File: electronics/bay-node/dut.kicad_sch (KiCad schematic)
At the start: 26 parts, among them J5 AUX, J6 CAM, Q2 2N7002, Q3 2N7002, U10 INA226AIDGSR, U9 TPS2553DBVR

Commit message: Bay node v0.4: In2 power only, re-placed, SMD JST PH, new GPIO map
Fabio's second round: signals / GND / power / signals.  With no signal
on In2, v0.3's placement left 13-18 connections unrouted, mostly GPIOs
leaving the module's left column for the right half.  Connectors and
module stay put; the DUT power block moves to the top right, LDO and
buttons to the top left, the muxes under the module, and each GPIO sits
on the module edge facing its destination (firmware devicetree, README
pin table and docs follow; check_pinmap.py passes).

pcbgen: fanout_nets gives every GND/supply pin its own locked via to
its plane before routing.  USB HS pairs redrawn for the new geometry
(J3 -> J4 skew 0.1 mm).  J1/J2/J5/J6 are now S*B-PH-SM4-TB, placed by
JLC (24 V and GND on solid islands with 4 vias each); UART test pads on
the bottom side.  J5 is a JST PH 6 (Fabio: SH too small).

ERC 0, DRC 0 errors / 0 warnings / 0 unconnected, parity 0 (Konnect).

Co-Authored-By: Claude Opus 5.5 <noreply@anthropic.com>
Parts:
- J5: footprint Connector_JST:JST_SH_SM06B-SRSS-TB_1x06-1MP_P1.00mm_Horizontal -> Connector_JST:JST_PH_S6B-PH-SM4-TB_1x06-1MP_P2.00mm_Horizontal; symbol Connector_Generic_MountingPin:Conn_01x06_MountingPin -> Connector_Generic:Conn_01x06; Alternative JST SM06B-SRSS-TB(LF)(SN) C160405 -> (none); LCSC C56123098 -> C265405; MPN XY-SM06B-SRSS-TB -> S6B-PH-SM4-TB(LF)(SN); Manufacturer XYECONN -> JST
- J6: footprint Connector_JST:JST_PH_S2B-PH-K_1x02_P2.00mm_Horizontal -> Connector_JST:JST_PH_S2B-PH-SM4-TB_1x02-1MP_P2.00mm_Horizontal; LCSC C173752 -> C295747; MPN S2B-PH-K-S(LF)(SN) -> S2B-PH-SM4-TB(LF)(SN)
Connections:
- net GND: no longer J5.MP (MountPin)
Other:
- note added: "AUX: UART + open-drain RESET / BOOT towards the DUT (JST PH 6)"
- note removed: "AUX: UART + open-drain RESET / BOOT towards the DUT (JST SH 6)"
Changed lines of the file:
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@@
 	(title_block
 		(title "Bay node — DUT power switch, monitor, AUX and camera power")
-		(rev "0.3")
+		(rev "0.4")
 		(company "hw-testing-rack")
 		(comment 1 "ESP32-S3 USB/IP host for one bay of the hw-testing-rack shelf")
@@
 	)
 	(symbol
-		(lib_id "Connector_Generic_MountingPin:Conn_01x06_MountingPin")
+		(lib_id "Connector_Generic:Conn_01x06")
 		(at 269.24 162.56 0)
 		(unit 1)
@@
 			)
 		)
-		(property "Footprint" "Connector_JST:JST_SH_SM06B-SRSS-TB_1x06-1MP_P1.00mm_Horizontal"
+		(property "Footprint" "Connector_JST:JST_PH_S6B-PH-SM4-TB_1x06-1MP_P2.00mm_Horizontal"
 			(at 269.24 162.56 0)
 			(effects
@@
 			)
 		)
-		(property "Description" "JST-SH 6-pin side entry"
+		(property "Description" "JST PH 6-pin, side entry, SMD"
 			(at 269.24 162.56 0)
 			(effects
@@
 			)
 		)
-		(property "MPN" "XY-SM06B-SRSS-TB"
+		(property "MPN" "S6B-PH-SM4-TB(LF)(SN)"
 			(at 269.24 162.56 0)
 			(effects
@@
 			)
 		)
-		(property "Manufacturer" "XYECONN"
-			(at 269.24 162.56 0)
-			(effects
-				(font
-					(size 1.27 1.27)
-				)
-				(hide yes)
-			)
-		)
-		(property "LCSC" "C56123098"
+		(property "Manufacturer" "JST"
 			(at 269.24 162.56 0)
 			(effects
@@
 			)
 		)
-		(property "Alternative" "JST SM06B-SRSS-TB(LF)(SN) C160405"
+		(property "LCSC" "C265405"
 			(at 269.24 162.56 0)
 			(effects
@@
 		(pin "6"
 		)
-		(pin "MP"
-		)
 		(instances
 			(project "bay-node"
@@
 		)
 	)
-	(wire
-		(pts
-			(xy 269.24 175.26)
-			(xy 269.24 177.8)
-		)
-		(stroke
-			(width 0)
-			(type default)
-		)
-	)
-	(symbol
-		(lib_id "power:GND")
-		(at 269.24 177.8 0)
-		(unit 1)
-		(exclude_from_sim no)
-		(in_bom yes)
-		(on_board yes)
-		(dnp no)
-		(fields_autoplaced yes)
-		(property "Reference" "#PWR05010"
-			(at 269.24 177.8 0)
-			(effects
-				(font
-					(size 1.27 1.27)
-				)
-				(hide yes)
-			)
-		)
-		(property "Value" "GND"
-			(at 269.24 181.61 0)
-			(effects
-				(font
-					(size 1.27 1.27)
-				)
-			)
-		)
-		(property "Footprint" ""
-			(at 269.24 177.8 0)
-			(effects
-				(font
-					(size 1.27 1.27)
-				)
-				(hide yes)
-			)
-		)
-		(property "Datasheet" ""
-			(at 269.24 177.8 0)
-			(effects
-				(font
-					(size 1.27 1.27)
-				)
-				(hide yes)
-			)
-		)
-		(property "Description" ""
-			(at 269.24 177.8 0)
-			(effects
-				(font
-					(size 1.27 1.27)
-				)
-				(hide yes)
-			)
-		)
-		(pin "1"
-		)
-		(instances
-			(project "bay-node"
-				(path "/76847c0c-2f76-566c-8109-428b2bf58b3f/a569d74c-9c07-57e9-a349-c34419c82b47"
-					(reference "#PWR05010")
-					(unit 1)
-				)
-			)
-		)
-	)
 	(symbol
 		(lib_id "Device:R")
@@
 		(dnp no)
 		(fields_autoplaced yes)
-		(property "Reference" "#PWR05011"
+		(property "Reference" "#PWR05010"
 			(at 220.98 182.88 0)
 			(effects
@@
 			(project "bay-node"
 				(path "/76847c0c-2f76-566c-8109-428b2bf58b3f/a569d74c-9c07-57e9-a349-c34419c82b47"
-					(reference "#PWR05011")
+					(reference "#PWR05010")
 					(unit 1)
 				)
@@
 		(dnp no)
 		(fields_autoplaced yes)
-		(property "Reference" "#PWR05012"
+		(property "Reference" "#PWR05011"
 			(at 220.98 208.28 0)
 			(effects
@@
 			(project "bay-node"
 				(path "/76847c0c-2f76-566c-8109-428b2bf58b3f/a569d74c-9c07-57e9-a349-c34419c82b47"
-					(reference "#PWR05012")
+					(reference "#PWR05011")
 					(unit 1)
 				)
@@
 		(dnp no)
 		(fields_autoplaced yes)
-		(property "Reference" "#PWR05013"
+		(property "Reference" "#PWR05012"
 			(at 205.74 185.42 0)
 			(effects
@@
 			(project "bay-node"
 				(path "/76847c0c-2f76-566c-8109-428b2bf58b3f/a569d74c-9c07-57e9-a349-c34419c82b47"
-					(reference "#PWR05013")
+					(reference "#PWR05012")
 					(unit 1)
 				)
@@
 		(dnp no)
 		(fields_autoplaced yes)
-		(property "Reference" "#PWR05014"
+		(property "Reference" "#PWR05013"
 			(at 205.74 210.82 0)
 			(effects
@@
 			(project "bay-node"
 				(path "/76847c0c-2f76-566c-8109-428b2bf58b3f/a569d74c-9c07-57e9-a349-c34419c82b47"
-					(reference "#PWR05014")
+					(reference "#PWR05013")
 					(unit 1)
 				)
@@
 			)
 		)
-		(property "Footprint" "Connector_JST:JST_PH_S2B-PH-K_1x02_P2.00mm_Horizontal"
+		(property "Footprint" "Connector_JST:JST_PH_S2B-PH-SM4-TB_1x02-1MP_P2.00mm_Horizontal"
 			(at 350.52 137.16 0)
 			(effects
@@
 			)
 		)
-		(property "Description" "JST PH 2-pin, side entry, 2 A"
+		(property "Description" "JST PH 2-pin, side entry, SMD, 2 A"
 			(at 350.52 137.16 0)
 			(effects
@@
 			)
 		)
-		(property "MPN" "S2B-PH-K-S(LF)(SN)"
+		(property "MPN" "S2B-PH-SM4-TB(LF)(SN)"
 			(at 350.52 137.16 0)
 			(effects
@@
 			)
 		)
-		(property "LCSC" "C173752"
+		(property "LCSC" "C295747"
 			(at 350.52 137.16 0)
 			(effects
@@
 		(dnp no)
 		(fields_autoplaced yes)
-		(property "Reference" "#PWR05015"
+		(property "Reference" "#PWR05014"
 			(at 45.72 73.66 0)
 			(effects
@@
 			(project "bay-node"
 				(path "/76847c0c-2f76-566c-8109-428b2bf58b3f/a569d74c-9c07-57e9-a349-c34419c82b47"
-					(reference "#PWR05015")
+					(reference "#PWR05014")
 					(unit 1)
 				)
@@
 		(dnp no)
 		(fields_autoplaced yes)
-		(property "Reference" "#PWR05016"
+		(property "Reference" "#PWR05015"
 			(at 203.2 73.66 0)
 			(effects
@@
 			(project "bay-node"
 				(path "/76847c0c-2f76-566c-8109-428b2bf58b3f/a569d74c-9c07-57e9-a349-c34419c82b47"
-					(reference "#PWR05016")
+					(reference "#PWR05015")
 					(unit 1)
 				)
@@
 		(dnp no)
 		(fields_autoplaced yes)
-		(property "Reference" "#PWR05017"
+		(property "Reference" "#PWR05016"
 			(at 187.96 60.96 0)
 			(effects
@@
 			(project "bay-node"
 				(path "/76847c0c-2f76-566c-8109-428b2bf58b3f/a569d74c-9c07-57e9-a349-c34419c82b47"
-					(reference "#PWR05017")
+					(reference "#PWR05016")
 					(unit 1)
 				)
@@
 		(dnp no)
 		(fields_autoplaced yes)
-		(property "Reference" "#PWR05018"
+		(property "Reference" "#PWR05017"
 			(at 254 45.72 0)
 			(effects
@@
 			(project "bay-node"
 				(path "/76847c0c-2f76-566c-8109-428b2bf58b3f/a569d74c-9c07-57e9-a349-c34419c82b47"
-					(reference "#PWR05018")
+					(reference "#PWR05017")
 					(unit 1)
 				)
@@
 		(dnp no)
 		(fields_autoplaced yes)
-		(property "Reference" "#PWR05019"
+		(property "Reference" "#PWR05018"
 			(at 220.98 132.08 0)
 			(effects
@@
 			(project "bay-node"
 				(path "/76847c0c-2f76-566c-8109-428b2bf58b3f/a569d74c-9c07-57e9-a349-c34419c82b47"
-					(reference "#PWR05019")
+					(reference "#PWR05018")
 					(unit 1)
 				)
@@
 		(dnp no)
 		(fields_autoplaced yes)
-		(property "Reference" "#PWR05020"
+		(property "Reference" "#PWR05019"
 			(at 304.8 137.16 0)
 			(effects
@@
 			(project "bay-node"
 				(path "/76847c0c-2f76-566c-8109-428b2bf58b3f/a569d74c-9c07-57e9-a349-c34419c82b47"
-					(reference "#PWR05020")
+					(reference "#PWR05019")
 					(unit 1)
 				)
@@
 		(dnp no)
 		(fields_autoplaced yes)
-		(property "Reference" "#PWR05021"
+		(property "Reference" "#PWR05020"
 			(at 340.36 144.78 0)
 			(effects
@@
 			(project "bay-node"
 				(path "/76847c0c-2f76-566c-8109-428b2bf58b3f/a569d74c-9c07-57e9-a349-c34419c82b47"
-					(reference "#PWR05021")
+					(reference "#PWR05020")
 					(unit 1)
 				)
@@
 		)
 	)
-	(text "AUX: UART + open-drain RESET / BOOT towards the DUT (JST SH 6)"
+	(text "AUX: UART + open-drain RESET / BOOT towards the DUT (JST PH 6)"
 		(exclude_from_sim no)
 		(at 173.99 124.46 0)

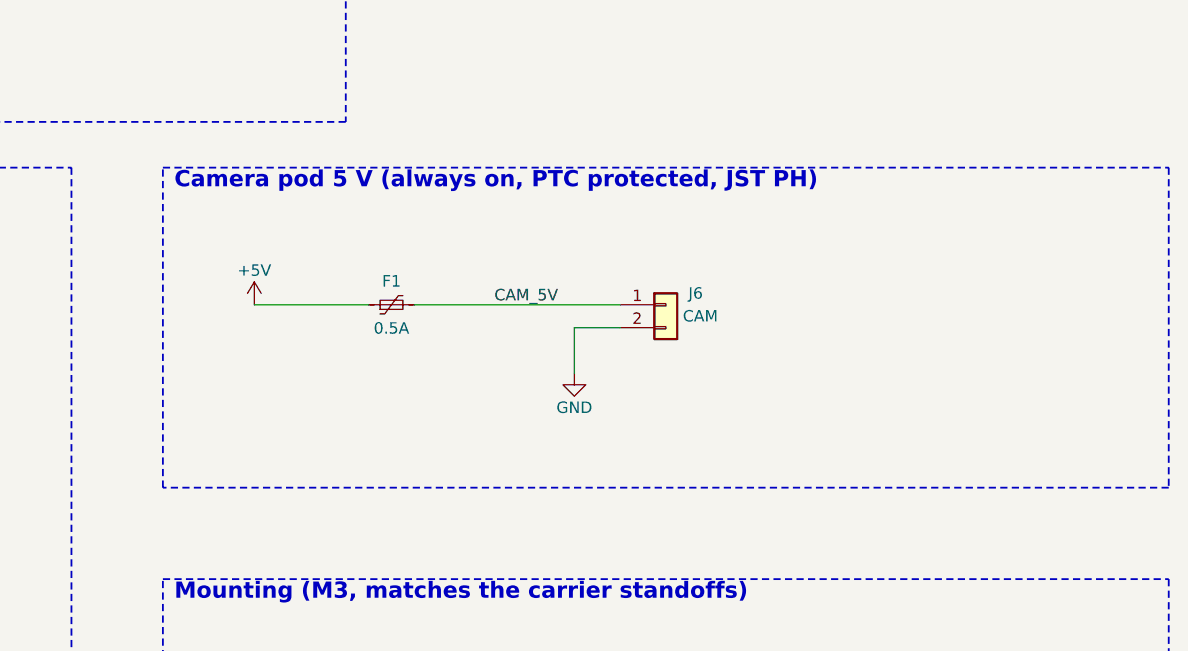
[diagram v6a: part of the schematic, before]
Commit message: Bay node: the bay's camera on J6, the WROOM-1-N8R8, the board 64 × 90
The user chose a camera per bay wired to its own node (camera hand-over,
option B: an Arducam Mega 3MP SPI, M12 ≈ 120°, and white LEDs on one PH 8
lead) and the ESP32-S3-WROOM-1-N8R8 for its 8 MB octal PSRAM, allowing
the board to grow at the rear.

- U3: WROOM-1-N8R8 (C2913201), the DevKitC-1-N8R8's module.  The board
  grew 10 mm at the rear (64 × 90): the layout, the holes and every
  pcb.bay_node y moved 10 mm with it, so the tray's standoffs and the
  fascia parts keep their place; the module's top edge is the new rear
  edge, its antenna band (6 mm, ±24 mm) kept clear.  bench footprint
  ESP32-S3-WROOM-1_NoEPVias: the stock one without its 0.2 mm in-pad
  vias, the pad on a GND island stitched around it.
- Pin map (the PSRAM takes IO35–37, no IO26/33/34 on a WROOM-1), the
  DevKitC-1 v1.1's as is: IO1/IO2 I²C, IO12 AUX_RST, IO21 AUX_RX, IO38 LED,
  IO42 POS_OUT; camera IO11 SCK, IO10 MOSI, IO9 MISO, IO8 CS, IO7 light.
- J6: PH 8 vertical (B8B) right of the PC pair, under J7; 33 Ω series,
  2 × USBLC6, CS 10k pull-up, MISO divider footprint (R35 DNP), the light
  on an AO3400A (100k gate pull-down), CAM_5V through the PTC.  A
  "Camera" schematic sheet.
- J5 (AUX): a vertical PH 6 (B6B), as the user asked.
- Re-routed.  ERC 0, DRC 0 / 0 unconnected / parity 0, JLC DFM: only the
  back-side test pads, 97/97 3D models (the B6B's EasyEDA STEP is not
  centred and turned).  The session import now also drops a via at the
  end of a dead branch, and the branch.  JLC corrections fitted for
  C2913201, C495548, C471518, C20917.
- BOM: the camera lines (B0434, 120° lens, LED strip, PH 8 lead) replace
  the XIAO / OV2640 / PH 2 lead; the node's post-quote changes +$18.91
  of parts, +$3 for the B6B type, +$1.83 for the larger board.
- firmware/README.md pin map: the new map.  check_pinmap waits for the
  firmware's devicetree (moved pins, camera).

Co-Authored-By: Claude Opus 5.5 <noreply@anthropic.com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
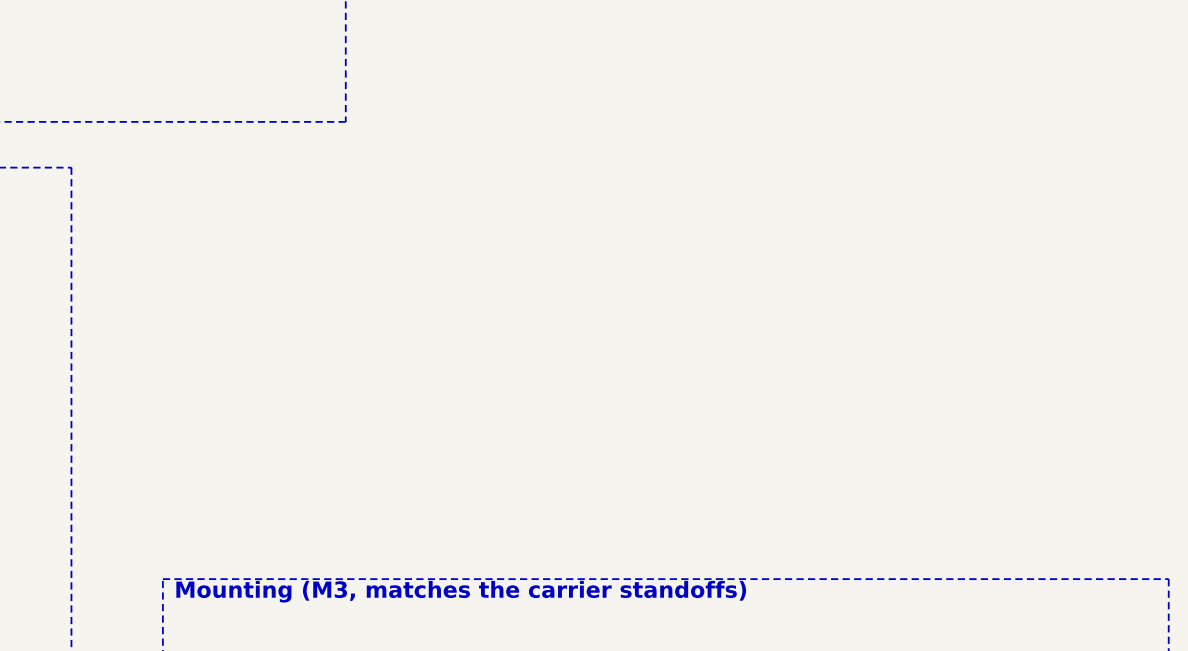
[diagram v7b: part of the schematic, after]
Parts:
- removed F1: 0.5A, Fuse:Fuse_1206_3216Metric, symbol Device:Polyfuse_Small
- removed J6: CAM, Connector_JST:JST_PH_S2B-PH-SM4-TB_1x02-1MP_P2.00mm_Horizontal, symbol Connector_Generic:Conn_01x02
- J5: footprint Connector_JST:JST_PH_S6B-PH-SM4-TB_1x06-1MP_P2.00mm_Horizontal -> Connector_JST:JST_PH_B6B-PH-SM4-TB_1x06-1MP_P2.00mm_Vertical; LCSC C265405 -> C471518; MPN S6B-PH-SM4-TB(LF)(SN) -> B6B-PH-SM4-TB(LF)(SN)
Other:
- note removed: "Camera pod 5 V (always on, PTC protected, JST PH)"
- title: Bay node — DUT power switch, monitor, AUX and camera power -> Bay node — DUT power switch, monitor and AUX
